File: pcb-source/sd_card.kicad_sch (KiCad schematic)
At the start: 4 parts, among them J14 MicroSD Card 0, J3 SD Card 1

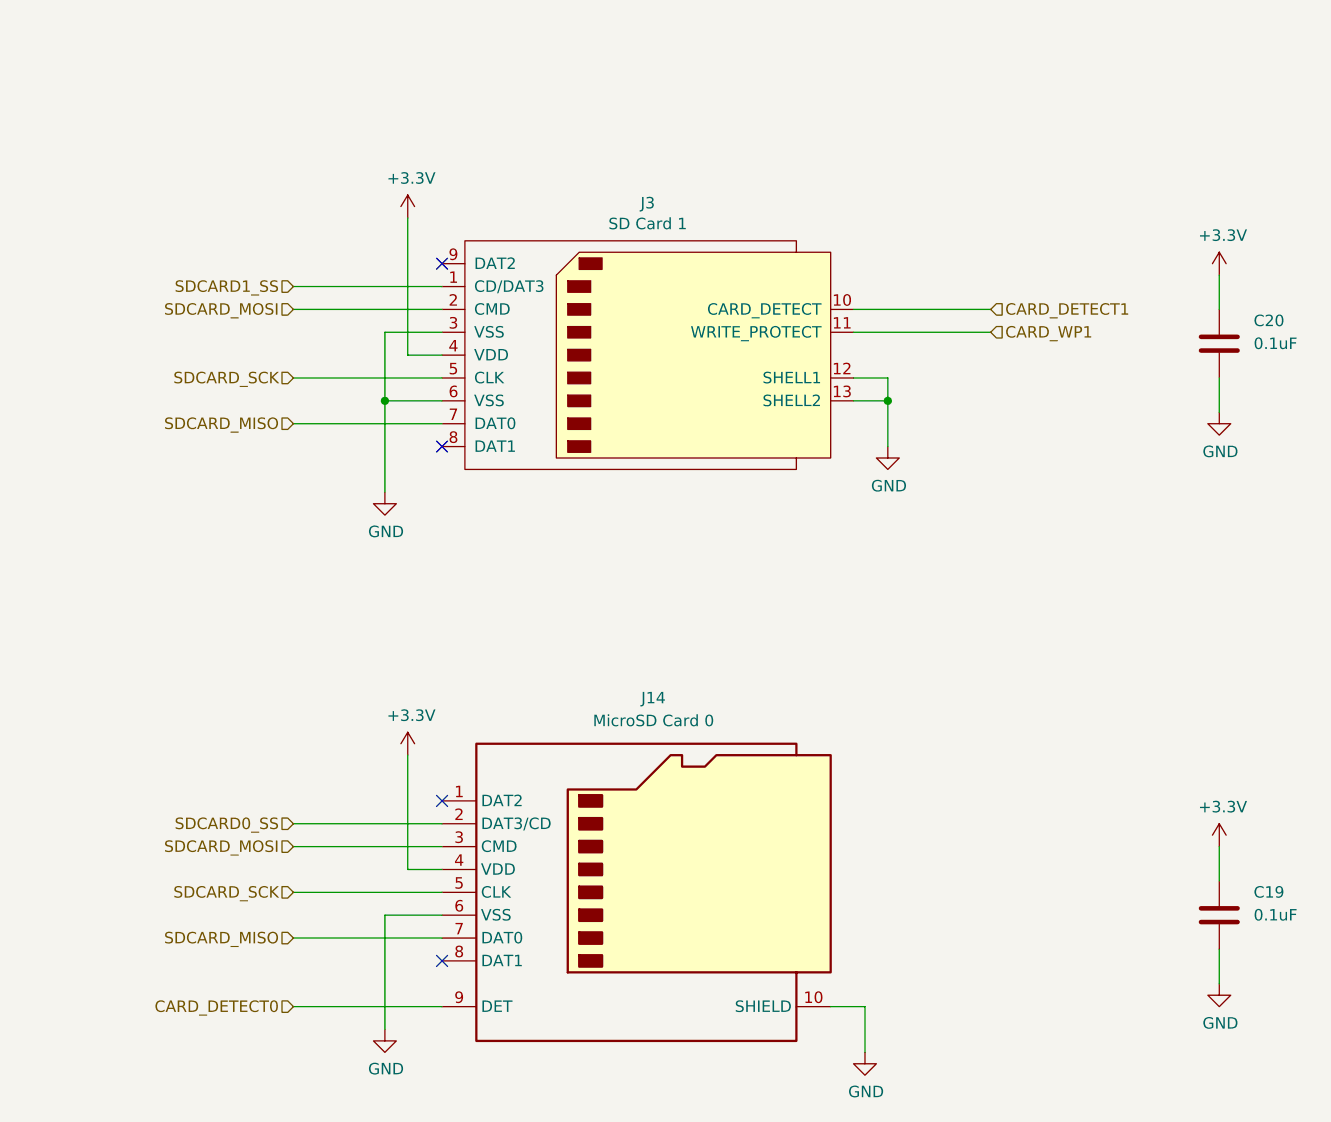
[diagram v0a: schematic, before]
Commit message: 1.2 version with 2 SPI buses
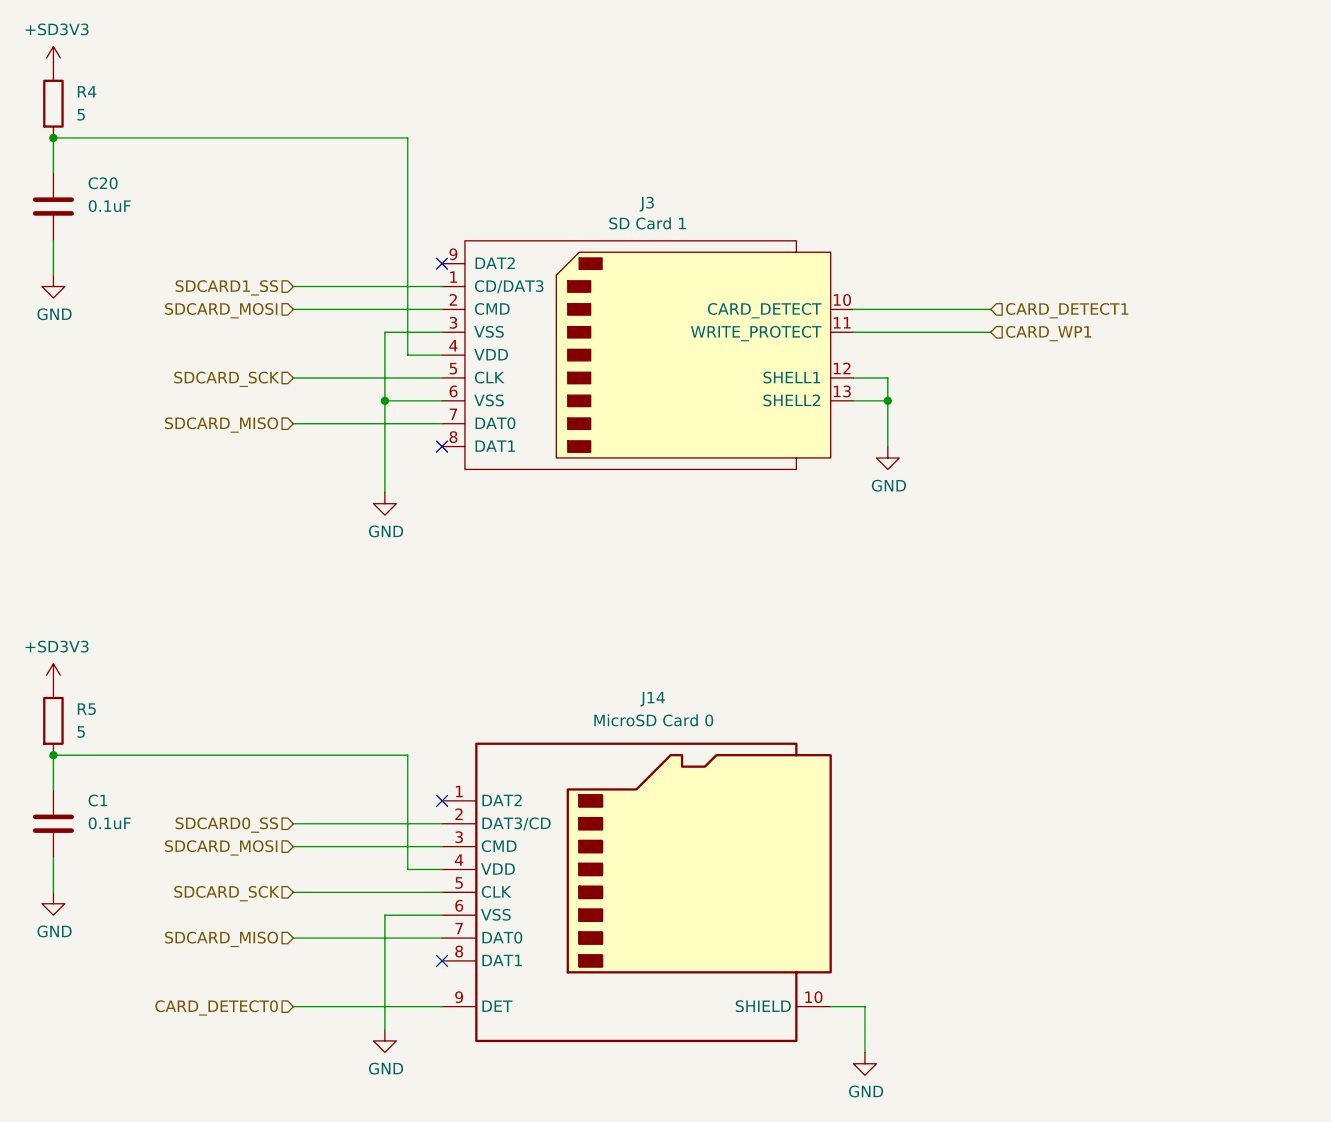
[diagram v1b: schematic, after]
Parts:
- removed C19: 0.1uF, Capacitor_SMD:C_0603_1608Metric, symbol Device:C
- added C1: 0.1uF, Capacitor_SMD:C_0603_1608Metric, symbol Device:C
- added R4, R5: 5, Resistor_SMD:R_0805_2012Metric, symbol Device:R
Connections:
- net GND: now also C1.2
- net +3V3: no longer names the net of C20.1, J3.4 (VDD)
- net +3V3: now also R4.2; no longer J14.4 (VDD)
- new net: C1.1, J14.4 (VDD), R5.2
- new net +SD3V3: R4.1, R5.1
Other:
- moved on the sheet: C20
